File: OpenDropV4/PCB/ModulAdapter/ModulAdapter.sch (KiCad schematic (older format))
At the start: 14 parts, among them J1 Mini_Dimm_244, J2 Conn_01x24_Female, P1 ScrewPad2, P13 ScrewPad1, P14 ScrewPad2, P15 ScrewPad2, P17 ScrewPad1, P2 ScrewPad2, U2 HV507, U4 HV507

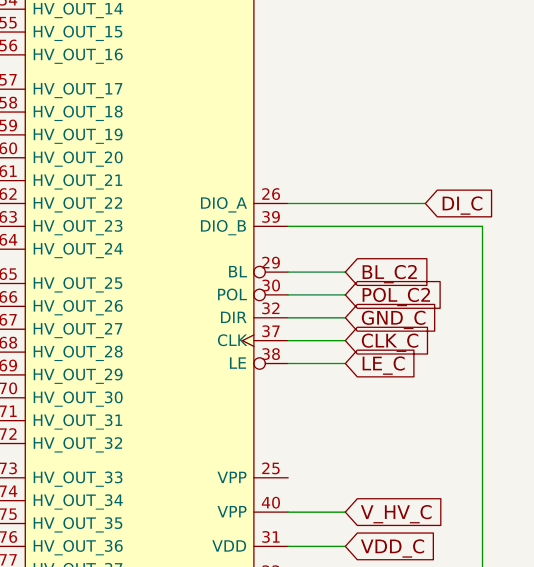
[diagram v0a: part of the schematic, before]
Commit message: Ready for second prototype round its not a synth
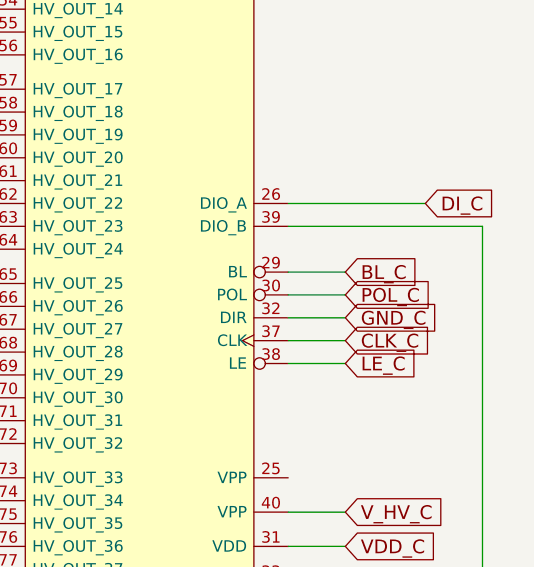
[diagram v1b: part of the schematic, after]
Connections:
- net BL_C2 is gone; now on net BL_C: U4.29 (BL)
- net POL_C2 is gone; now on net POL_C: U4.30 (POL)
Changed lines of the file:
@@
 VDD_C
 Text GLabel 16850 3600 2    60   Input ~ 0
-BL_C2
+BL_C
 Text GLabel 16850 3900 2    60   Input ~ 0
 CLK_C
@@
 LE_C
 Text GLabel 16850 3700 2    60   Input ~ 0
-POL_C2
+POL_C
 Text GLabel 16850 3800 2    60   Input ~ 0
 GND_C
